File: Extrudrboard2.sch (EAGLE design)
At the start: 7 parts, among them U1 SN74HC138N

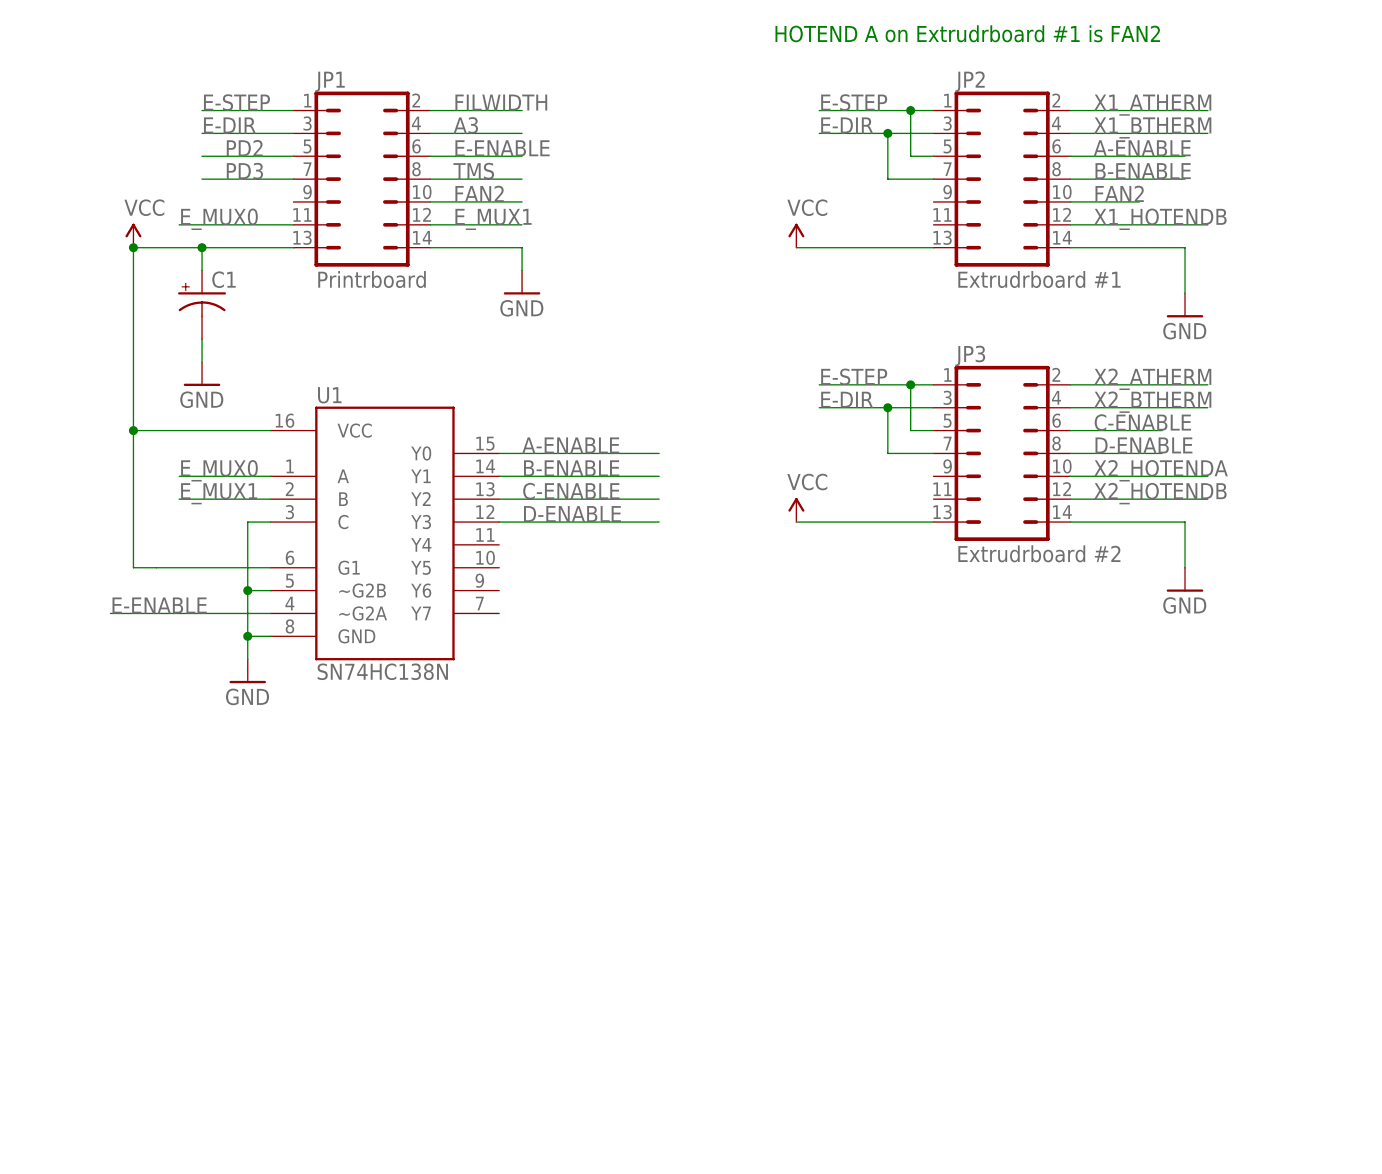
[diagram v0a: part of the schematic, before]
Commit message: Multiplex STEP instead of ENABLE.
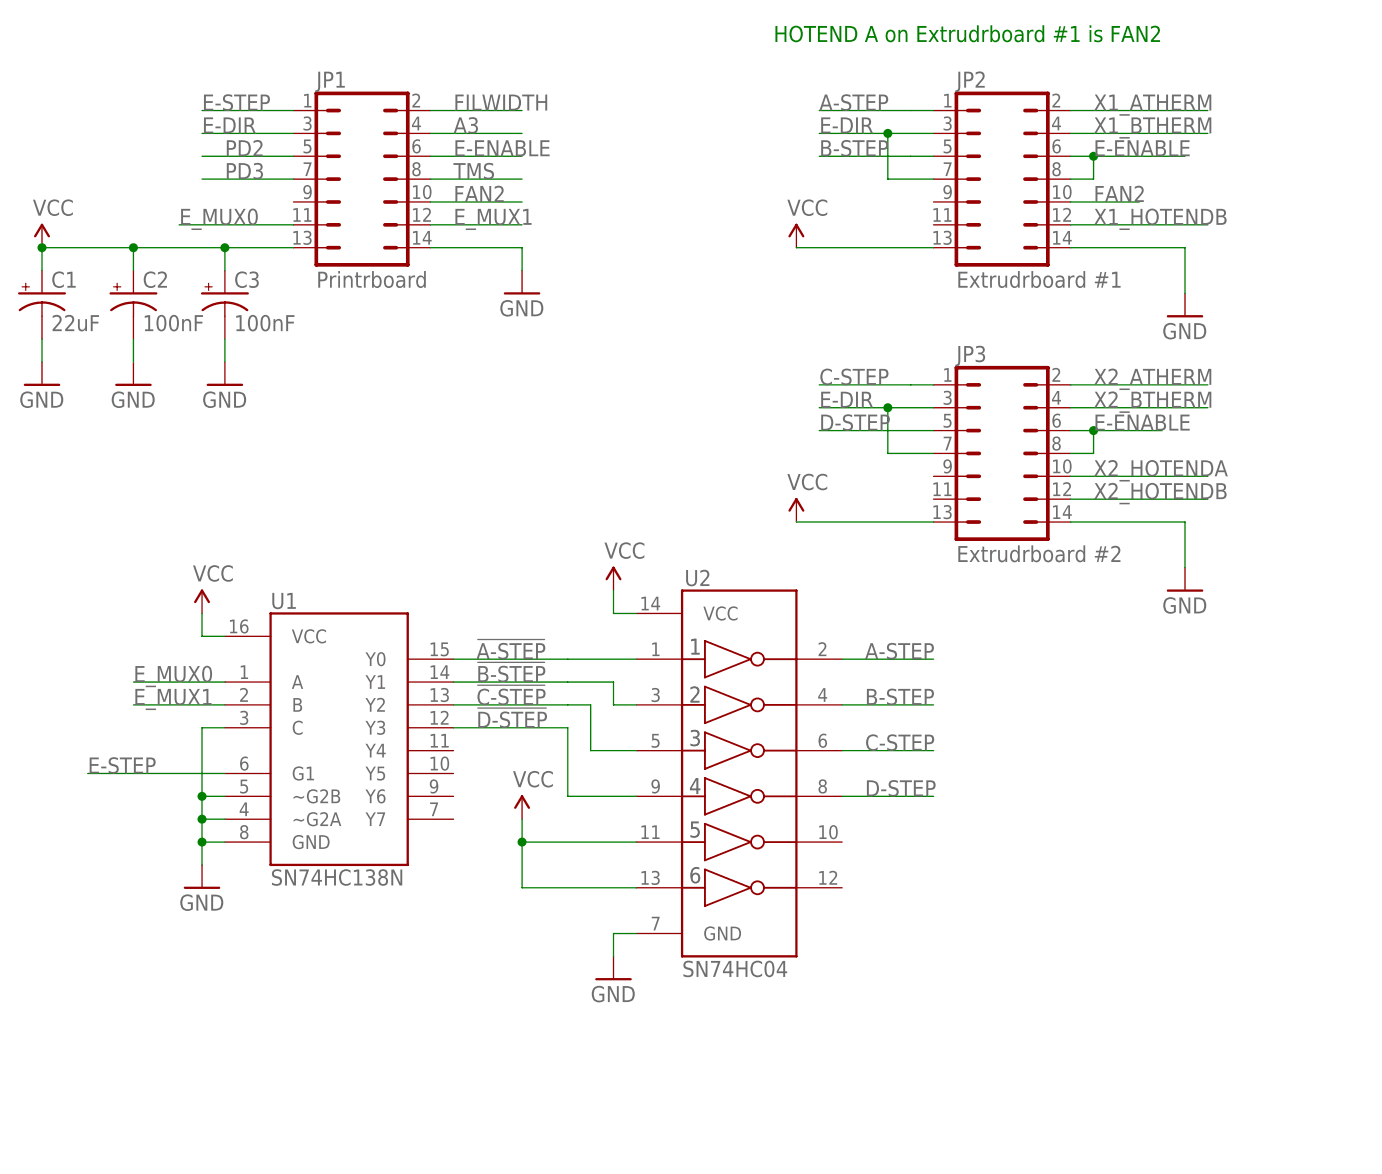
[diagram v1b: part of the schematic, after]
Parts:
- added C2, C3: 100nF, SparkFun:CAP_POLPTH2
- added U2: SN74HC04, SparkFun:74HC04_HEX_INVERTER
- C1: value (none) -> 22uF
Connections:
- removed net A-ENABLE: JP2.6, U1.Y0
- removed net B-ENABLE: JP2.8, U1.Y1
- removed net C-ENABLE: JP3.6, U1.Y2
- removed net D-ENABLE: JP3.8, U1.Y3
- new net !A-STEP: U1.Y0, U2.1A
- new net !B-STEP: U1.Y1, U2.2A
- new net !C-STEP: U1.Y2, U2.3A
- new net !D-STEP: U1.Y3, U2.4A
- new net A-STEP: JP2.1, U2.1Y
- new net B-STEP: JP2.5, U2.2Y
- new net C-STEP: JP3.1, U2.3Y
- new net D-STEP: JP3.5, U2.4Y
- net E-ENABLE: now also JP2.6, JP2.8, JP3.6, JP3.8; no longer U1.~G2A
- net E-STEP: now also U1.G1; no longer JP2.1, JP2.5, JP3.1, JP3.5
- net GND: now also C2.-, C3.-, U1.~G2A, U2.GND
- net VCC: now also C2.+, C3.+, U2.5A, U2.6A, U2.VCC; no longer U1.G1
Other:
- moved on the sheet: C1, U1

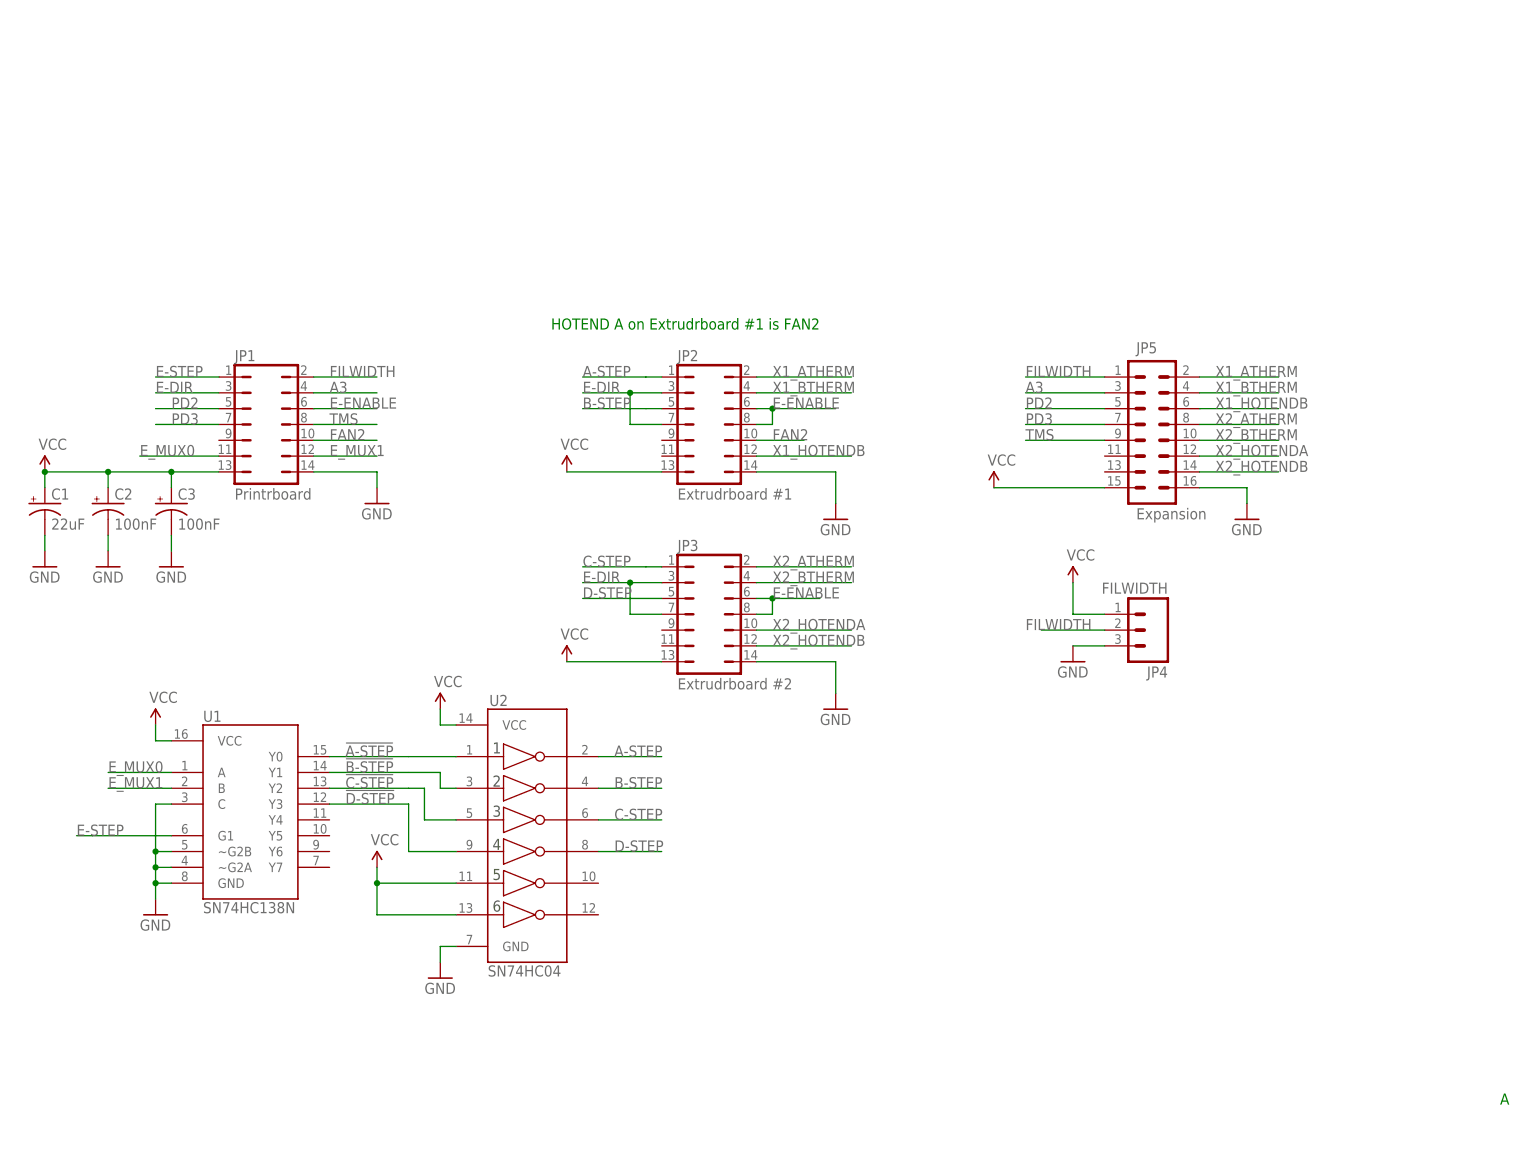
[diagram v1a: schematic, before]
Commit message: Rename Extrudrboard to Extrudrboard2 for clarity.
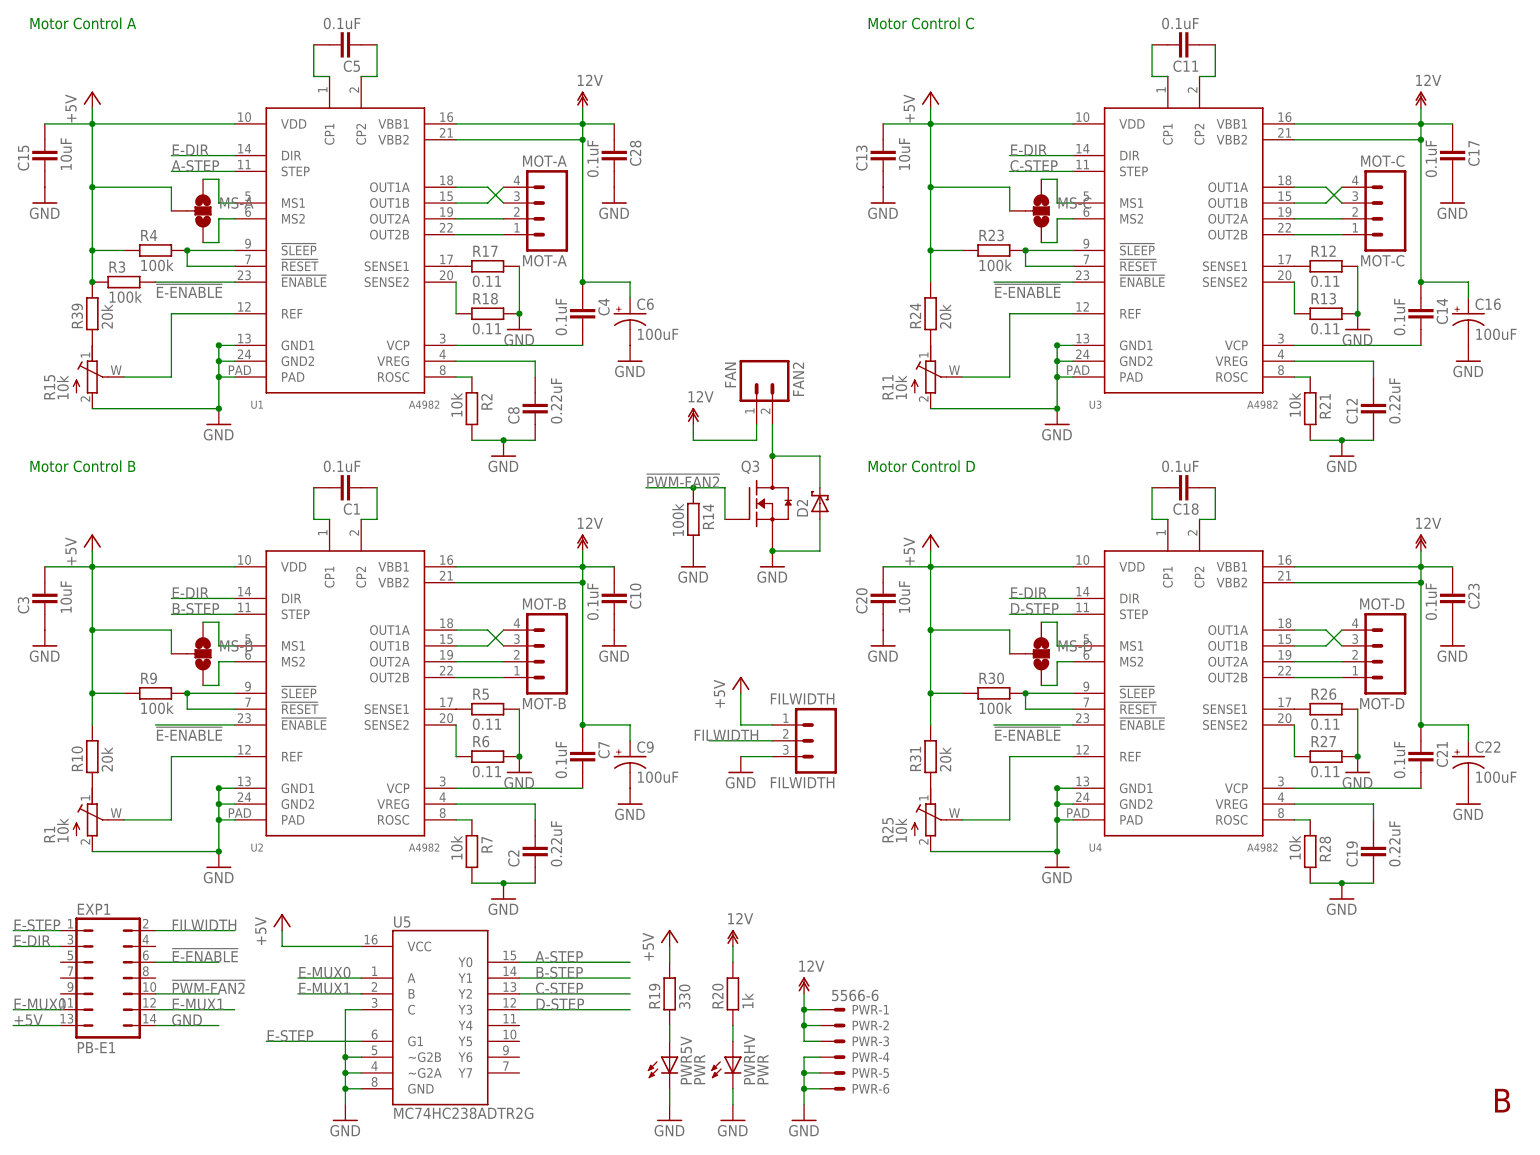
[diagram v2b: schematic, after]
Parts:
- removed JP1: Printrboard, printrbot:JP7Q
- removed JP2: Extrudrboard #1, printrbot:JP7Q
- removed JP3: Extrudrboard #2, printrbot:JP7Q
- removed JP4: FILWIDTH, SparkFun:M03PTH
- removed JP5: Expansion, SparkFun:M08X2
- added C10, C11, C14, C17, C18, C21, C23, C28, C4, C5, C7: 0.1uF, ipc-7351-capacitor:CAPACITOR_0805
- added C12, C19, C8: 0.22uF, ipc-7351-capacitor:CAPACITOR_0805
- added C13, C15, C20: 10uF, ipc-7351-capacitor:CAPACITOR_0805
- added C16, C22, C6, C9: 100uF, rcl:CPOL-USD
- added D2: SCH-DIODESMA, printrbot:SCH-DIODESMA
- added EXP1: PB-E1, printrbot:JP7Q
- added FAN2: FAN, SparkFun:M02PTH
- added FILWIDTH: FILWIDTH, SparkFun:M03PTH
- added MOT-A: MOT-A, SparkFun:M04POLAR
- added MOT-B: MOT-B, SparkFun:M04POLAR
- added MOT-C: MOT-C, SparkFun:M04POLAR
- added MOT-D: MOT-D, SparkFun:M04POLAR
- added MS-A, MS-B, MS-C, MS-D: (no value), printrbot:SOLDERJUMPER_2WAYCONNECTED
- added PWR: 5566-6, printrbot:5566-6
- added PWR5V, PWRHV: PWR, led:LEDCHIP-LED0805
- added Q3: RFP30N06LE, ipc-7351-transistor:MOSFET-NCH_SOT-23
- added R1, R11, R15, R25: 10k, printrbot:RTRIM-ST-4EA
- added R10, R24, R31, R39: 20k, ipc-7351-resistor:RESISTOR_0805
- added R12, R13, R17, R18, R26, R27, R5, R6: 0.11, ipc-7351-resistor:RESISTOR_0805
- added R14, R23, R3, R30, R4, R9: 100k, ipc-7351-resistor:RESISTOR_0805
- added R19: 330, ipc-7351-resistor:RESISTOR_0805
- added R2, R21, R28, R7: 10k, ipc-7351-resistor:RESISTOR_0805
- added R20: 1k, ipc-7351-resistor:RESISTOR_0805
- added U3, U4: A4982, printrbot:A4982
- added U5: MC74HC238ADTR2G, mux:M74HC238DT
- C1: value 22uF -> 0.1uF; device SparkFun:CAP_POLPTH1 -> ipc-7351-capacitor:CAPACITOR_0805
- C2: value 100nF -> 0.22uF; device SparkFun:CAP_POLPTH2 -> ipc-7351-capacitor:CAPACITOR_0805
- C3: value 100nF -> 10uF; device SparkFun:CAP_POLPTH2 -> ipc-7351-capacitor:CAPACITOR_0805
- U1: value SN74HC138N -> A4982; device SparkFun:M74HC238 -> printrbot:A4982
- U2: value SN74HC04 -> A4982; device SparkFun:74HC04_HEX_INVERTER -> printrbot:A4982
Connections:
- removed net !A-STEP: U1.Y0, U2.1A
- removed net !B-STEP: U1.Y1, U2.2A
- removed net !C-STEP: U1.Y2, U2.3A
- removed net !D-STEP: U1.Y3, U2.4A
- removed net A3: JP1.4, JP5.3
- removed net E-ENABLE: JP1.6, JP2.6, JP2.8, JP3.6, JP3.8
- removed net E_MUX0: JP1.11, U1.A
- removed net E_MUX1: JP1.12, U1.B
- removed net FAN2: JP1.10, JP2.10
- removed net PD2: JP1.5, JP5.5
- removed net PD3: JP1.7, JP5.7
- removed net TMS: JP1.8, JP5.9
- removed net VCC: C1.+, C2.+, C3.+, JP1.13, JP2.13, JP3.13, JP4.1, JP5.15, U1.VCC, U2.5A, U2.6A, U2.VCC
- removed net X1_ATHERM: JP2.2, JP5.2
- removed net X1_BTHERM: JP2.4, JP5.4
- removed net X1_HOTENDB: JP2.12, JP5.6
- removed net X2_ATHERM: JP3.2, JP5.8
- removed net X2_BTHERM: JP3.4, JP5.10
- removed net X2_HOTENDA: JP3.10, JP5.12
- removed net X2_HOTENDB: JP3.12, JP5.14
- new net !E-ENABLE: EXP1.6, R3.2, U1.!ENABLE, U2.!ENABLE, U3.!ENABLE, U4.!ENABLE
- new net !PWM-FAN2: EXP1.10, Q3.G, R14.1
- new net +5V: C13.2, C15.2, C20.2, C3.2, EXP1.13, FILWIDTH.1, MS-A.2, MS-B.2, MS-C.2, MS-D.2, R10.2, R19.2, R23.1, R24.2, R3.1, R30.1, R31.2, R39.2, R4.1, R9.1, U1.VDD, U2.VDD, U3.VDD, U4.VDD, U5.VCC
- new net 12V: C10.1, C14.1, C16.+, C17.1, C21.1, C22.+, C23.1, C28.1, C4.1, C6.+, C7.1, C9.+, FAN2.1, PWR-1.S, PWR-2.S, PWR-3.S, R20.2, U1.VBB1, U1.VBB2, U2.VBB1, U2.VBB2, U3.VBB1, U3.VBB2, U4.VBB1, U4.VBB2
- new net E-MUX0: EXP1.11, U5.A
- new net E-MUX1: EXP1.12, U5.B
- new net N$1: C1.2, U2.CP1
- new net N$10: MOT-A.3, U1.OUT1A
- new net N$11: C5.2, U1.CP1
- new net N$12: C5.1, U1.CP2
- new net N$13: R2.1, U1.ROSC
- new net N$14: R17.1, U1.SENSE1
- new net N$15: R18.1, U1.SENSE2
- new net N$16: C4.2, U1.VCP
- new net N$17: MOT-A.4, U1.OUT1B
- new net N$18: R15.S, U1.REF
- new net N$19: C8.2, U1.VREG
- new net N$2: C1.1, U2.CP2
- new net N$20: MOT-A.2, U1.OUT2A
- new net N$21: R4.2, U1.!RESET, U1.!SLEEP
- new net N$22: MS-B.1, U2.MS1
- new net N$23: MOT-A.1, U1.OUT2B
- new net N$24: MS-B.3, U2.MS2
- new net N$25: MOT-B.3, U2.OUT1A
- new net N$26: MOT-B.4, U2.OUT1B
- new net N$27: MS-A.1, U1.MS1
- new net N$28: MS-A.3, U1.MS2
- new net N$29: MOT-B.2, U2.OUT2A
- new net N$3: R5.1, U2.SENSE1
- new net N$30: MOT-B.1, U2.OUT2B
- new net N$31: R1.A, R10.1
- new net N$33: PWR5V.A, R19.1
- new net N$34: PWRHV.A, R20.1
- new net N$35: C11.2, U3.CP1
- new net N$36: C11.1, U3.CP2
- new net N$37: R12.1, U3.SENSE1
- new net N$38: R13.1, U3.SENSE2
- new net N$39: R11.S, U3.REF
- new net N$4: R6.1, U2.SENSE2
- new net N$40: R21.1, U3.ROSC
- new net N$41: C12.2, U3.VREG
- new net N$42: R23.2, U3.!RESET, U3.!SLEEP
- new net N$43: C14.2, U3.VCP
- new net N$44: MS-C.1, U3.MS1
- new net N$45: MS-C.3, U3.MS2
- new net N$46: MOT-C.3, U3.OUT1A
- new net N$47: MOT-C.4, U3.OUT1B
- new net N$48: MOT-C.2, U3.OUT2A
- new net N$49: MOT-C.1, U3.OUT2B
- new net N$5: R1.S, U2.REF
- new net N$50: R11.A, R24.1
- new net N$51: C18.2, U4.CP1
- new net N$52: C18.1, U4.CP2
- new net N$53: R26.1, U4.SENSE1
- new net N$54: R27.1, U4.SENSE2
- new net N$55: R25.S, U4.REF
- new net N$56: R28.1, U4.ROSC
- new net N$57: C19.2, U4.VREG
- new net N$58: R30.2, U4.!RESET, U4.!SLEEP
- new net N$59: C21.2, U4.VCP
- new net N$6: R7.1, U2.ROSC
- new net N$60: MS-D.1, U4.MS1
- new net N$61: MS-D.3, U4.MS2
- new net N$62: MOT-D.3, U4.OUT1A
- new net N$63: MOT-D.4, U4.OUT1B
- new net N$64: MOT-D.2, U4.OUT2A
- new net N$65: MOT-D.1, U4.OUT2B
- new net N$66: R25.A, R31.1
- new net N$67: D2.C, FAN2.2, Q3.D
- new net N$69: R15.A, R39.1
- new net N$7: C2.2, U2.VREG
- new net N$8: R9.2, U2.!RESET, U2.!SLEEP
- new net N$9: C7.2, U2.VCP
- net A-STEP: now also U1.STEP, U5.Y0; no longer JP2.1, U2.1Y
- net B-STEP: now also U2.STEP, U5.Y1; no longer JP2.5, U2.2Y
- net C-STEP: now also U3.STEP, U5.Y2; no longer JP3.1, U2.3Y
- net D-STEP: now also U4.STEP, U5.Y3; no longer JP3.5, U2.4Y
- net E-DIR: now also EXP1.3, U1.DIR, U2.DIR, U3.DIR, U4.DIR; no longer JP1.3, JP2.3, JP2.7, JP3.3, JP3.7
- net E-STEP: now also EXP1.1, U5.G1; no longer JP1.1, U1.G1
- net FILWIDTH: now also EXP1.2, FILWIDTH.2; no longer JP1.2, JP4.2, JP5.1
- net GND: now also C10.2, C12.1, C13.1, C15.1, C16.-, C17.2, C19.1, C2.1, C20.1, C22.-, C23.2, C28.2, C3.1, C6.-, C8.1, C9.-, D2.A, EXP1.14, FILWIDTH.3, PWR-4.S, PWR-5.S, PWR-6.S, PWR5V.C, PWRHV.C, Q3.S, R1.E, R11.E, R12.2, R13.2, R14.2, R15.E, R17.2, R18.2, R2.2, R21.2, R25.E, R26.2, R27.2, R28.2, R5.2, R6.2, R7.2, U1.GND1, U1.GND2, U1.PAD, U2.GND1, U2.GND2, U2.PAD, U3.GND1, U3.GND2, U3.PAD, U4.GND1, U4.GND2, U4.PAD, U5.C, U5.GND, U5.~G2A, U5.~G2B; no longer C1.-, C2.-, C3.-, JP1.14, JP2.14, JP3.14, JP4.3, JP5.16, U1.C, U1.GND, U1.~G2A, U1.~G2B, U2.GND
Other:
- note added: "B"
- note added: "Motor Control A"
- note added: "Motor Control B"
- note added: "Motor Control C"
- note added: "Motor Control D"
- note removed: "A"
- note removed: "HOTEND A on Extrudrboard #1 is FAN2"
